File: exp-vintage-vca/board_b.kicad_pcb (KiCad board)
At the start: 2 copper layers, 30 x 110 mm, 46 parts, among them J10 Conn_01x10_Socket, J12 Conn_01x04_Socket, J15 Conn_02x08_Odd_Even, J9 Conn_01x10_Socket, Q1 BC556, Q2 BC556, U1 TL074, U3 LM13700

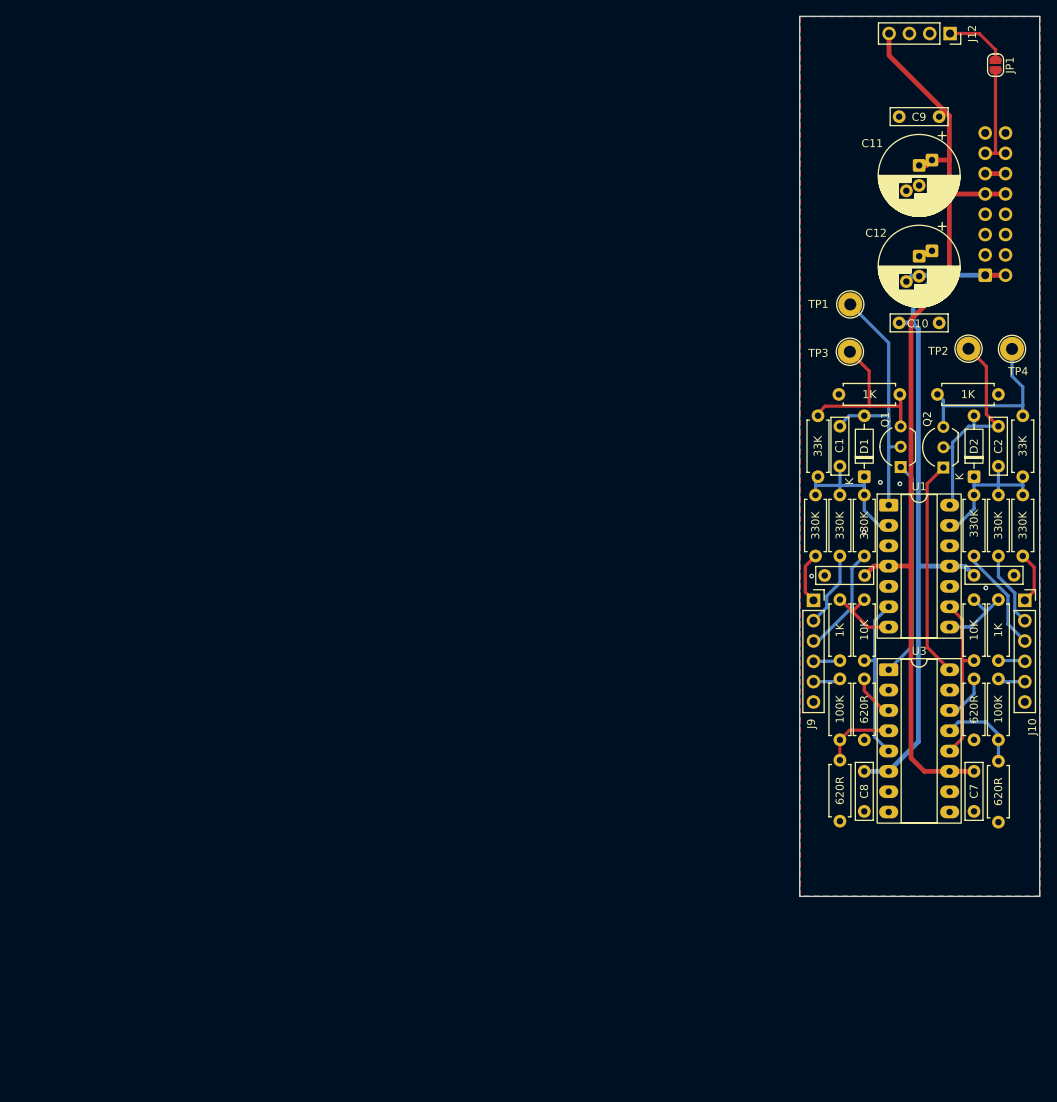
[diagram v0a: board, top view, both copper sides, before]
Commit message: Exponential VCA ver. 1.2
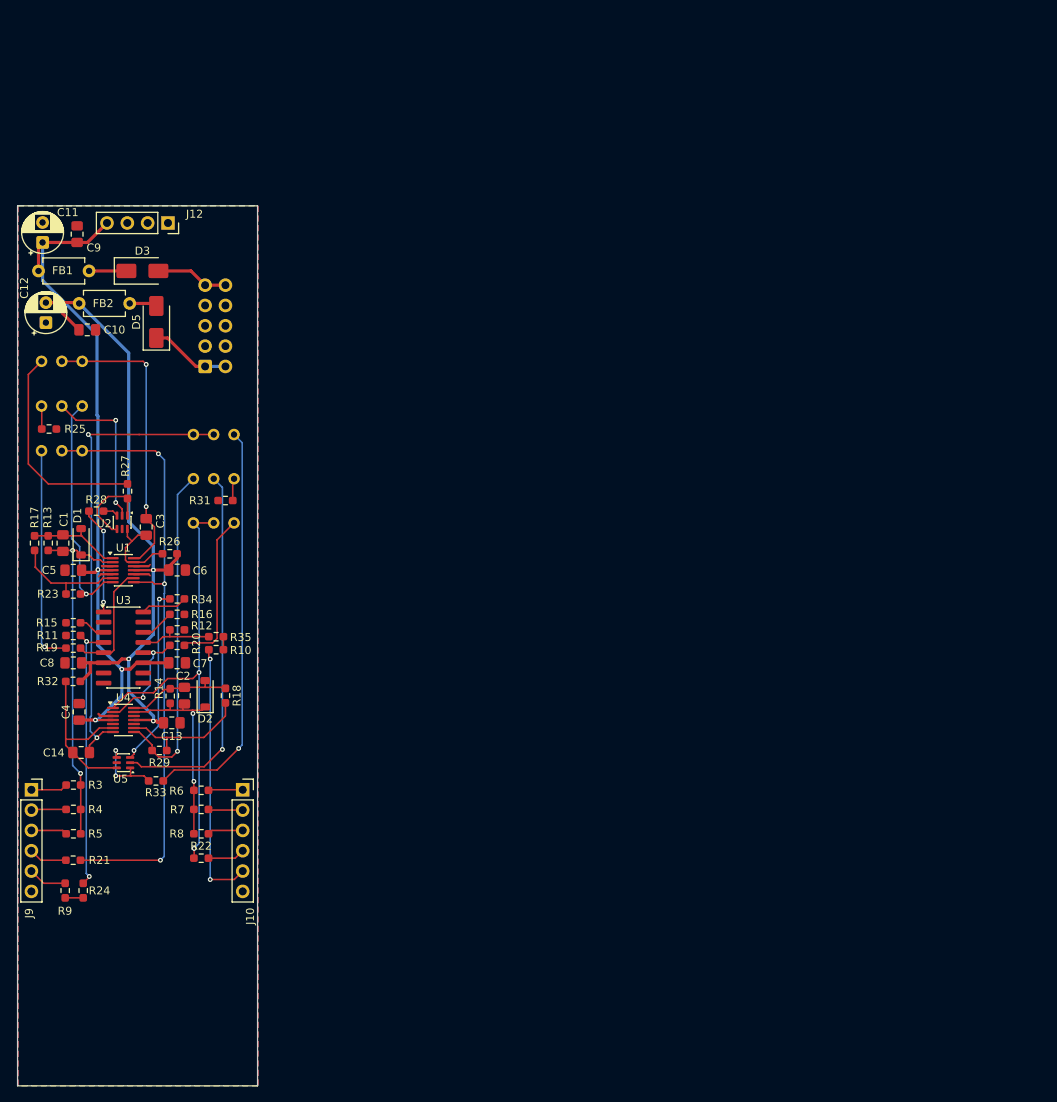
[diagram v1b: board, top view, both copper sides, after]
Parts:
- removed JP1: SolderJumper_2_Open, Jumper:SolderJumper-2_P1.3mm_Open_RoundedPad1.0x1.5mm
- removed Q1, Q2: BC556, Package_TO_SOT_THT:TO-92_Inline_Wide
- removed TP1, TP2, TP3, TP4: TestPoint, TestPoint:TestPoint_Loop_D2.54mm_Drill1.5mm_Beaded
- added C13: 100n, Capacitor_SMD:C_0805_2012Metric_Pad1.18x1.45mm_HandSolder, F.Cu at (55.0, 108.3)
- added C14: 100pF, Capacitor_SMD:C_0805_2012Metric_Pad1.18x1.45mm_HandSolder, F.Cu at (43.7, 112.0)
- added C3: 100pF, Capacitor_SMD:C_0805_2012Metric_Pad1.18x1.45mm_HandSolder, F.Cu at (51.8, 83.8)
- added C4: 100n, Capacitor_SMD:C_0805_2012Metric_Pad1.18x1.45mm_HandSolder, F.Cu at (43.4, 106.9)
- added D3: SS14, Diode_SMD:D_SMA, F.Cu at (51.3, 51.8)
- added D5: SS14, Diode_SMD:D_SMA, F.Cu at (53.1, 58.2)
- added FB1: FerriteBead_Small, linear_vintage_vca:Ferrite_Bead_5mm_3.5mm_Horizontal, F.Cu at (38.4, 51.8)
- added FB2: FerriteBead_Small, linear_vintage_vca:Ferrite_Bead_5mm_3.5mm_Horizontal, F.Cu at (43.4, 55.9)
- added R23: 330K, Resistor_SMD:R_0603_1608Metric_Pad0.98x0.95mm_HandSolder, F.Cu at (42.7, 92.2)
- added R24: 10K, Resistor_SMD:R_0603_1608Metric_Pad0.98x0.95mm_HandSolder, F.Cu at (43.9, 129.3)
- added R25: 10, Resistor_SMD:R_0603_1608Metric_Pad0.98x0.95mm_HandSolder, F.Cu at (39.7, 71.6)
- added R26: 2Meg, Resistor_SMD:R_0603_1608Metric_Pad0.98x0.95mm_HandSolder, F.Cu at (54.8, 87.2)
- added R27: 10K, Resistor_SMD:R_0603_1608Metric_Pad0.98x0.95mm_HandSolder, F.Cu at (49.5, 79.3)
- added R28: 20K, Resistor_SMD:R_0603_1608Metric_Pad0.98x0.95mm_HandSolder, F.Cu at (45.6, 81.8)
- added R29: 330K, Resistor_SMD:R_0603_1608Metric_Pad0.98x0.95mm_HandSolder, F.Cu at (53.5, 111.8)
- added R31: 10, Resistor_SMD:R_0603_1608Metric_Pad0.98x0.95mm_HandSolder, F.Cu at (61.7, 80.5)
- added R32: 2Meg, Resistor_SMD:R_0603_1608Metric_Pad0.98x0.95mm_HandSolder, F.Cu at (42.7, 103.1)
- added R33: 10K, Resistor_SMD:R_0603_1608Metric_Pad0.98x0.95mm_HandSolder, F.Cu at (53.0, 115.6)
- added R34: 20K, Resistor_SMD:R_0603_1608Metric_Pad0.98x0.95mm_HandSolder, F.Cu at (55.7, 92.8)
- added R35: 10K, Resistor_SMD:R_0603_1608Metric_Pad0.98x0.95mm_HandSolder, F.Cu at (60.6, 97.5)
- added RV10: 20K, Potentiometer_THT:Potentiometer_Bourns_3296W_Vertical, B.Cu at (62.8, 72.3)
- added RV5: 1k, Potentiometer_THT:Potentiometer_Bourns_3296W_Vertical, B.Cu at (38.7, 68.7)
- added RV6: 1k, Potentiometer_THT:Potentiometer_Bourns_3296W_Vertical, B.Cu at (62.8, 77.8)
- added RV7: 20K, Potentiometer_THT:Potentiometer_Bourns_3296W_Vertical, B.Cu at (38.7, 74.3)
- added RV8: 20K, Potentiometer_THT:Potentiometer_Bourns_3296W_Vertical, B.Cu at (62.8, 83.3)
- added RV9: 20k, Potentiometer_THT:Potentiometer_Bourns_3296W_Vertical, B.Cu at (38.7, 63.1)
- added U2: BC857BS, Package_TO_SOT_SMD:SOT-363_SC-70-6, F.Cu at (48.8, 83.2)
- added U4: TL074, linear_vintage_vca:SOT-23-THIN-14_2x4.2mm_P0.5mm, F.Cu at (49.0, 108.0)
- added U5: BC857BS, Package_TO_SOT_SMD:SOT-363_SC-70-6, F.Cu at (49.0, 113.3)
- C1, C2: value 100n -> 1n; footprint Capacitor_THT:C_Rect_L7.0mm_W2.0mm_P5.00mm -> Capacitor_SMD:C_0805_2012Metric_Pad1.18x1.45mm_HandSolder
- C10, C5, C6, C7, C8, C9: footprint Capacitor_THT:C_Rect_L7.0mm_W2.0mm_P5.00mm -> Capacitor_SMD:C_0805_2012Metric_Pad1.18x1.45mm_HandSolder
- C11, C12: value 47uF -> 10uF; footprint Capacitor_THT:CP_Radial_D10.0mm_P2.50mm_P5.00mm -> Capacitor_THT:CP_Radial_D5.0mm_P2.50mm
- D1, D2: footprint Diode_THT:D_DO-35_SOD27_P7.62mm_Horizontal -> Diode_SMD:D_SOD-123
- J15: footprint Connector_IDC:IDC-Header_2x08_P2.54mm_Vertical -> Connector_IDC:IDC-Header_2x05_P2.54mm_Vertical
- R10, R13, R14, R19, R20, R21, R22, R3, R4, R5, R6, R7, R8, R9: footprint linear_vintage_vca:R_Axial_DIN0207_L6.3mm_D2.5mm_P7.62mm_Horizontal -> Resistor_SMD:R_0603_1608Metric_Pad0.98x0.95mm_HandSolder
- R11, R12, R15, R16: value 620R -> 680R; footprint linear_vintage_vca:R_Axial_DIN0207_L6.3mm_D2.5mm_P7.62mm_Horizontal -> Resistor_SMD:R_0603_1608Metric_Pad0.98x0.95mm_HandSolder
- R17, R18: value 1K -> 330K; footprint linear_vintage_vca:R_Axial_DIN0207_L6.3mm_D2.5mm_P7.62mm_Horizontal -> Resistor_SMD:R_0603_1608Metric_Pad0.98x0.95mm_HandSolder
- U1: footprint Package_DIP:DIP-14_W7.62mm_Socket_LongPads -> linear_vintage_vca:SOT-23-THIN-14_2x4.2mm_P0.5mm
- U3: footprint Package_DIP:DIP-16_W7.62mm_Socket_LongPads -> Package_SO:SOIC-16_3.9x9.9mm_P1.27mm
- moved R14 110.0 mm to (54.8, 105.0)
- moved C11 110.0 mm to (38.9, 48.3), turned to 90 degrees
- moved R17 109.7 mm to (37.9, 85.8), turned to -90 degrees
- moved C12 109.5 mm to (39.3, 58.3), turned to 90 degrees
- moved C9 108.8 mm to (43.2, 47.2), turned to 90 degrees
- moved R6 106.8 mm to (58.7, 116.7), turned to 180 degrees
- moved C10 106.5 mm to (44.5, 59.2)
- moved C2 105.7 mm to (56.6, 104.9)
- moved R5 104.8 mm to (42.7, 122.2), turned to 0 degrees
- moved R22 104.8 mm to (58.7, 125.2), turned to 0 degrees
- moved C6 104.6 mm to (55.7, 89.2)
- moved R7 104.6 mm to (58.7, 119.1), turned to 180 degrees
- moved R12 104.0 mm to (55.7, 96.7), turned to 0 degrees
- moved R8 102.7 mm to (58.7, 122.2), turned to 180 degrees
- moved R21 101.2 mm to (42.7, 125.5), turned to 180 degrees
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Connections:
- J12 pad 1: Net-(J12-Pin_1) -> GND
- J15 pad 1: -12V -> Net-(D5-K)
- J15 pad 10: +12V -> Net-(D3-A)
- J15 pad 2: -12V -> Net-(D5-K)
- J15 pad 9: +12V -> Net-(D3-A)
- R10 pad 2: Net-(U3A--) -> Net-(R10-Pad2)
- R13 pad 2: Net-(Q1-E) -> Net-(D1-A)
- R14 pad 2: Net-(Q2-E) -> Net-(D2-A)
- R17 pad 1: Net-(Q1-E) -> Net-(D1-A)
- R17 pad 2: GND -> Net-(U1B--)
- R18 pad 1: Net-(Q2-E) -> Net-(D2-A)
- R18 pad 2: GND -> Net-(U4C--)
- R19 pad 1: Net-(U1B--) -> Net-(U1C--)
- R20 pad 1: Net-(U1C--) -> Net-(U4A--)
- R21 pad 1: Net-(R19-Pad2) -> Net-(R21-Pad1)
- R22 pad 1: Net-(R20-Pad2) -> Net-(R22-Pad1)
- R9 pad 2: Net-(U3C--) -> Net-(R24-Pad1)
- U1 pad 13: Net-(D2-K) -> Net-(U1D--)
- U1 pad 14: Net-(D2-A) -> Net-(C3-Pad2)
- U1 pad 7: Net-(R19-Pad2) -> Net-(R23-Pad2)
- U1 pad 8: Net-(R20-Pad2) -> Net-(R21-Pad1)
- U3 pad 12: Net-(U1C--) -> Net-(U4A--)
- U3 pad 5: Net-(U1B--) -> Net-(U1C--)
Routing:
- net Net-(R21-Pad1): track 0.00 -> 77.5 mm, vias 0 -> 3
- net Net-(C14-Pad2): track 0.00 -> 58.7 mm, vias 0 -> 2
- net Net-(R22-Pad1): track 0.00 -> 57.6 mm, vias 0 -> 2
- net Net-(R33-Pad2): track 0.00 -> 51.0 mm, vias 0 -> 1
- net Net-(U5A-B1): track 0.00 -> 46.9 mm, vias 0 -> 1
- net Net-(R29-Pad2): track 0.00 -> 42.4 mm, vias 0 -> 1
- net Net-(C3-Pad2): track 0.00 -> 36.9 mm, vias 0 -> 2
- net Net-(J10-Pin_5): track 3.44 -> 33.4 mm, vias 0 -> 2
- net +12V: track 122.7 -> 92.9 mm, vias 0 -> 3
- net Net-(R23-Pad2): track 0.00 -> 29.4 mm, vias 0 -> 1
- net Net-(R27-Pad2): track 0.00 -> 26.9 mm
- net Net-(D1-A): track 36.9 -> 11.8 mm
- net Net-(U3C--): track 9.16 -> 34.0 mm, vias 0 -> 2
- net Net-(D1-K): track 20.0 -> 44.6 mm, vias 0 -> 2
- net Net-(Q2-E): track 23.3 -> 0.00 mm
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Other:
- board text added: "1. Input at 10V p2p 2. Set CV at 5V 3. Trim SHAPE until output at 10V p2p (unity gain) 4. Set CV at 1V 5. Trim SLOPE until output at 625mV 6. Repeat from step 2 7. Set CV at 6V 8. Use TRIM to cap gain slightly above unity"
- board text added: "SHAPE"
- board text added: "SLOPE"
- board text added: "TRIM"
- board text added: "VCA-2 Exp ver. 1.1 BC857BS 3/2026"
